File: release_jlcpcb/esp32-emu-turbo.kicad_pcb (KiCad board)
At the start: 4 copper layers, 160 x 75 mm, 71 parts, among them J1 USB-C-16P, J3 JST-PH-2P, J4 FPC-40P-0.5mm, SW1 SW-SMD-5.1x5.1, SW10 SW-SMD-5.1x5.1, SW11 SW-SMD-5.1x5.1, SW12 SW-SMD-5.1x5.1, SW13 SW-SMD-5.1x5.1, SW2 SW-SMD-5.1x5.1, SW3 SW-SMD-5.1x5.1, SW4 SW-SMD-5.1x5.1, SW5 SW-SMD-5.1x5.1, SW6 SW-SMD-5.1x5.1, SW7 SW-SMD-5.1x5.1, SW8 SW-SMD-5.1x5.1, SW9 SW-SMD-5.1x5.1, U1 ESP32-S3-WROOM-1-N16R8, U2 ESOP-8, U3 SOT-223, U5 SOP-16, U6 TF-01A

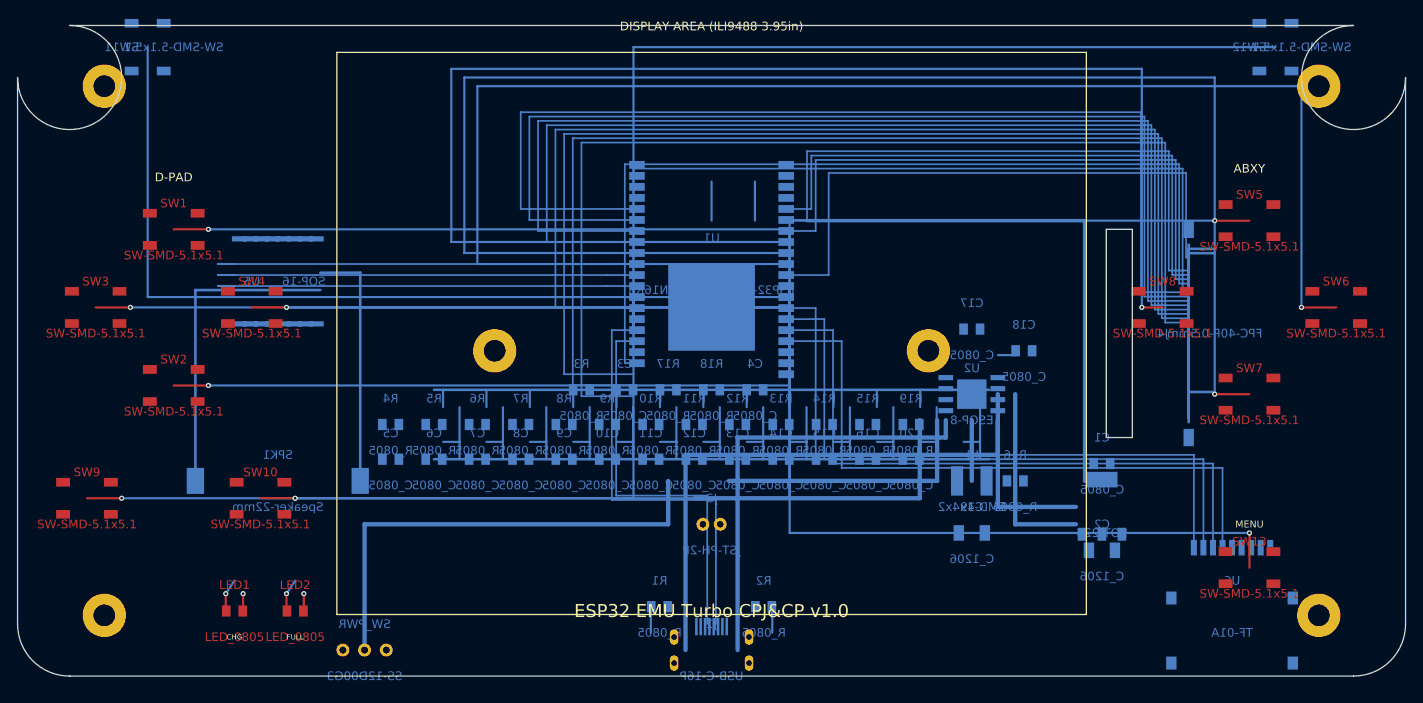
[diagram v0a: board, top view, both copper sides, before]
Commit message: v1.3: Fix trace shorts, DRC clean, zone fill verified
PCB Routing Fixes:
- Fix 3 trace shorts: reroute SD_MOSI/SD_MISO with B.Cu vertical bypass
  columns (x=120, x=118) to avoid FPC zone conflicts with LCD_D4/D6/BTN_Y
- Fix 3 FPC slot crossings: SD_CLK/SD_CS bypass at x=114/x=112,
  button channels shifted to y=48+ (below slot y range)
- Fix drill spacing: move +3V3 ESP32 via to (93,22.5), update DRC rule
  to JLCPCB 4-layer actual capability (0.25mm edge-to-edge)

Verification Results (all PASS):
- DRC: 0 errors (trace width, via dims, edge clearance, spacing, drill)
- Short circuit: 0 trace shorts
- Zone fill: 7 filled polygons (In1_Cu GND, In2_Cu +3V3/+5V)
- Gerber sizes: In1_Cu=258KB, In2_Cu=271KB
- Schematic/PCB consistency: 64 JLCPCB components matched

Production Files Updated:
- Regenerated Gerbers with zone fill via Docker kicad-cli
- Updated release_jlcpcb/ (BOM, CPL, Gerbers, PCB, ZIP)
- Updated documentation (README, pcb.md, manufacturing.md)
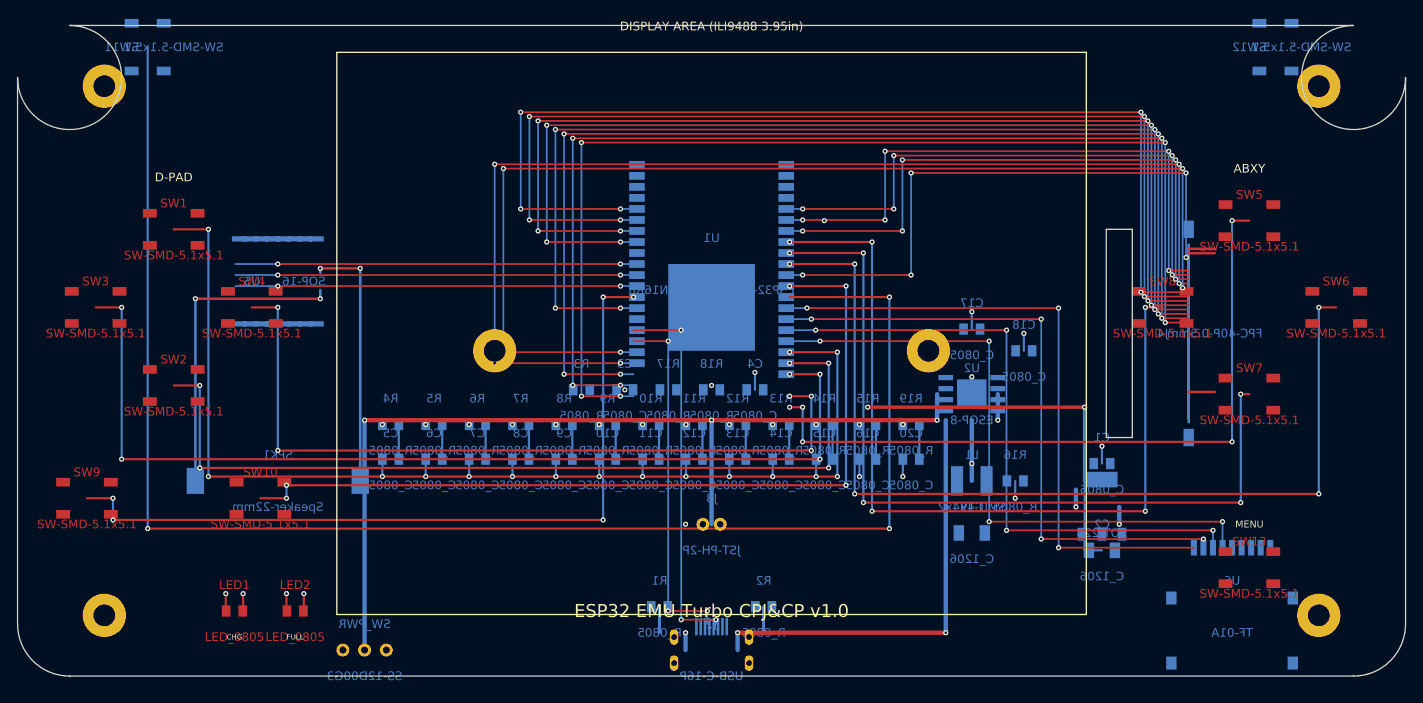
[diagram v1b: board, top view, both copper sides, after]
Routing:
- net BAT+: track 85.5 -> 1012.9 mm, vias 0 -> 73
- net LCD_D0: track 121.9 -> 504.2 mm, vias 0 -> 20
- net LCD_D3: track 118.2 -> 343.1 mm, vias 0 -> 15
- net BTN_X: track 190.6 -> 4.00 mm, vias 1 -> 0
- net BTN_B: track 186.9 -> 4.00 mm, vias 1 -> 0
- net BTN_Y: track 174.4 -> 4.00 mm, vias 1 -> 0
- net LCD_D7: track 126.0 -> 0.00 mm
- net LCD_D6: track 127.2 -> 253.2 mm, vias 0 -> 10
- net LCD_D4: track 123.3 -> 0.00 mm
- net LCD_D1: track 120.7 -> 0.00 mm
- net BTN_R: track 112.5 -> 0.00 mm
- net LCD_WR: track 102.7 -> 0.00 mm
- net LCD_RD: track 98.9 -> 0.00 mm
- net BTN_LEFT: track 93.6 -> 4.00 mm, vias 1 -> 0
- net BTN_START: track 92.1 -> 4.00 mm, vias 1 -> 0
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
